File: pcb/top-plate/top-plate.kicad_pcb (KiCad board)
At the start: 2 copper layers, 285.8 x 114.3 mm, 81 parts

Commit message: Add the remaining M2 holes for the top plate
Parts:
- added REF**: MountingHole_2.2mm_M2, MountingHole:MountingHole_2.2mm_M2, F.Cu at (38.1, 30.3)
- added REF**: MountingHole_2.2mm_M2, MountingHole:MountingHole_2.2mm_M2, F.Cu at (285.7, 126.4)
- added REF**: MountingHole_2.2mm_M2, MountingHole:MountingHole_2.2mm_M2, F.Cu at (38.1, 126.4)
- added REF**: MountingHole_2.2mm_M2, MountingHole:MountingHole_2.2mm_M2, F.Cu at (285.7, 30.3)
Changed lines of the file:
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@@
     (fp_line (start -6.5 7) (end 6.499672 7.000007) (layer "Edge.Cuts") (width 0.1))
     (fp_arc (start 53 -6) (mid 53.353553 -5.853553) (end 53.5 -5.5) (layer "Edge.Cuts") (width 0.1))
-    (fp_arc (start 6.999672 5.500007) (mid 7.146108 5.146445) (end 7.499672 5.000007) (layer "Edge.Cuts") (width 0.1))
+    (fp_arc (start 6.999672 5.500007) (mid 7.146107 5.146441) (end 7.499672 5.000007) (layer "Edge.Cuts") (width 0.1))
     (fp_arc (start 47.975 6.5) (mid 48.328553 6.646447) (end 48.475 7) (layer "Edge.Cuts") (width 0.1))
     (fp_arc (start 46.25 5) (mid 46.603553 5.146447) (end 46.75 5.5) (layer "Edge.Cuts") (width 0.1))
@@
     (fp_arc (start -53 6.5) (mid -53.353553 6.353553) (end -53.5 6) (layer "Edge.Cuts") (width 0.1))
     (fp_arc (start -7 -5.5) (mid -7.146447 -5.146447) (end -7.5 -5) (layer "Edge.Cuts") (width 0.1))
-    (fp_arc (start 6.999672 6.500007) (mid 6.853215 6.853551) (end 6.499672 7.000007) (layer "Edge.Cuts") (width 0.1))
+    (fp_arc (start 6.999672 6.500007) (mid 6.853214 6.853548) (end 6.499672 7.000007) (layer "Edge.Cuts") (width 0.1))
     (fp_arc (start 51.775 7) (mid 51.921447 6.646447) (end 52.275 6.5) (layer "Edge.Cuts") (width 0.1))
     (fp_arc (start -53.5 -5.5) (mid -53.353553 -5.853553) (end -53 -6) (layer "Edge.Cuts") (width 0.1))
@@
     (fp_arc (start -7 -6.5) (mid -6.853553 -6.853553) (end -6.5 -7) (layer "Edge.Cuts") (width 0.1))
   )
+  (footprint "MountingHole:MountingHole_2.2mm_M2" (layer "F.Cu")
+    (at 38.1 30.3)
+    (descr "Mounting Hole 2.2mm, no annular, M2")
+    (tags "mounting hole 2.2mm no annular m2")
+    (attr exclude_from_pos_files exclude_from_bom)
+    (fp_text reference "REF**" (at 0 -3.2) (layer "F.SilkS")
+      (effects (font (size 1 1) (thickness 0.15)))
+    )
+    (fp_text value "MountingHole_2.2mm_M2" (at 0 3.2) (layer "F.Fab")
+      (effects (font (size 1 1) (thickness 0.15)))
+    )
+    (fp_text user "${REFERENCE}" (at 0 0) (layer "F.Fab")
+      (effects (font (size 1 1) (thickness 0.15)))
+    )
+    (fp_circle (center 0 0) (end 2.2 0) (layer "Cmts.User") (width 0.15) (fill none))
+    (fp_circle (center 0 0) (end 2.45 0) (layer "F.CrtYd") (width 0.05) (fill none))
+    (pad "" np_thru_hole circle (at 0 0) (size 2.2 2.2) (drill 2.2) (layers *.Cu *.Mask))
+  )
   (footprint "bschwind_slots:mx_top_plate_1.00u" (layer "F.Cu")
     (at 228.6 66.67505)
@@
     (fp_arc (start -6.5 6.990924) (mid -6.853553 6.844477) (end -7 6.490924) (layer "Edge.Cuts") (width 0.1))
   )
+  (footprint "MountingHole:MountingHole_2.2mm_M2" (layer "F.Cu")
+    (at 285.7 126.4)
+    (descr "Mounting Hole 2.2mm, no annular, M2")
+    (tags "mounting hole 2.2mm no annular m2")
+    (attr exclude_from_pos_files exclude_from_bom)
+    (fp_text reference "REF**" (at 0 -3.2) (layer "F.SilkS")
+      (effects (font (size 1 1) (thickness 0.15)))
+    )
+    (fp_text value "MountingHole_2.2mm_M2" (at 0 3.2) (layer "F.Fab")
+      (effects (font (size 1 1) (thickness 0.15)))
+    )
+    (fp_text user "${REFERENCE}" (at 0 0) (layer "F.Fab")
+      (effects (font (size 1 1) (thickness 0.15)))
+    )
+    (fp_circle (center 0 0) (end 2.2 0) (layer "Cmts.User") (width 0.15) (fill none))
+    (fp_circle (center 0 0) (end 2.45 0) (layer "F.CrtYd") (width 0.05) (fill none))
+    (pad "" np_thru_hole circle (at 0 0) (size 2.2 2.2) (drill 2.2) (layers *.Cu *.Mask))
+  )
   (footprint "bschwind_slots:mx_top_plate_1.00u" (layer "F.Cu")
     (at 171.45 28.57505)
@@
     (fp_arc (start -7 -6.5) (mid -6.853553 -6.853553) (end -6.5 -7) (layer "Edge.Cuts") (width 0.1))
   )
+  (footprint "MountingHole:MountingHole_2.2mm_M2" (layer "F.Cu")
+    (at 38.1 126.4)
+    (descr "Mounting Hole 2.2mm, no annular, M2")
+    (tags "mounting hole 2.2mm no annular m2")
+    (attr exclude_from_pos_files exclude_from_bom)
+    (fp_text reference "REF**" (at 0 -3.2) (layer "F.SilkS")
+      (effects (font (size 1 1) (thickness 0.15)))
+    )
+    (fp_text value "MountingHole_2.2mm_M2" (at 0 3.2) (layer "F.Fab")
+      (effects (font (size 1 1) (thickness 0.15)))
+    )
+    (fp_text user "${REFERENCE}" (at 0 0) (layer "F.Fab")
+      (effects (font (size 1 1) (thickness 0.15)))
+    )
+    (fp_circle (center 0 0) (end 2.2 0) (layer "Cmts.User") (width 0.15) (fill none))
+    (fp_circle (center 0 0) (end 2.45 0) (layer "F.CrtYd") (width 0.05) (fill none))
+    (pad "" np_thru_hole circle (at 0 0) (size 2.2 2.2) (drill 2.2) (layers *.Cu *.Mask))
+  )
   (footprint "bschwind_slots:mx_top_plate_1.00u" (layer "F.Cu")
     (at 219.075 47.62505)
@@
     (fp_arc (start 6.5 -7) (mid 6.853553 -6.853553) (end 7 -6.5) (layer "Edge.Cuts") (width 0.1))
   )
-  (footprint "bschwind_slots:mx_top_plate_1.00u" (layer "F.Cu")
+  (footprint "MountingHole:MountingHole_2.2mm_M2" (layer "F.Cu")
+    (at 285.7 30.3)
+    (descr "Mounting Hole 2.2mm, no annular, M2")
+    (tags "mounting hole 2.2mm no annular m2")
+    (attr exclude_from_pos_files exclude_from_bom)
+    (fp_text reference "REF**" (at 0 -3.2) (layer "F.SilkS")
+      (effects (font (size 1 1) (thickness 0.15)))
+    )
+    (fp_text value "MountingHole_2.2mm_M2" (at 0 3.2) (layer "F.Fab")
+      (effects (font (size 1 1) (thickness 0.15)))
+    )
+    (fp_text user "${REFERENCE}" (at 0 0) (layer "F.Fab")
+      (effects (font (size 1 1) (thickness 0.15)))
+    )
+    (fp_circle (center 0 0) (end 2.2 0) (layer "Cmts.User") (width 0.15) (fill none))
+    (fp_circle (center 0 0) (end 2.45 0) (layer "F.CrtYd") (width 0.05) (fill none))
+    (pad "" np_thru_hole circle (at 0 0) (size 2.2 2.2) (drill 2.2) (layers *.Cu *.Mask))
+  )
+  (footprint "bschwind_slots:mx_top_plate_1.00u" (layer "F.Cu")

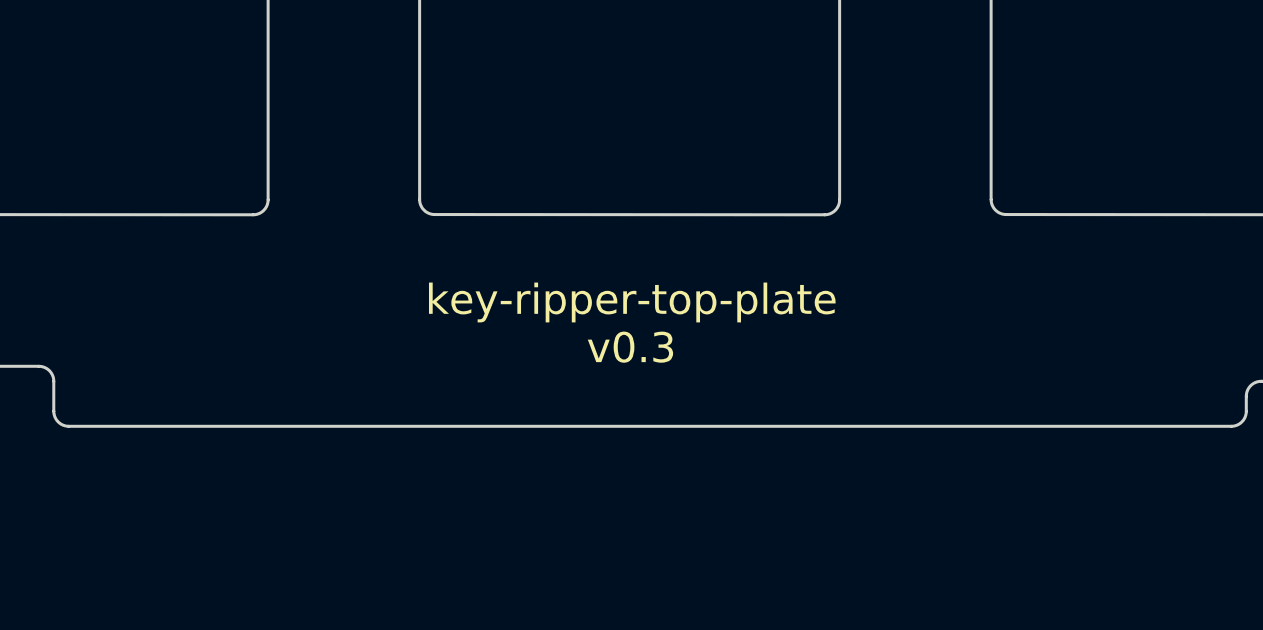
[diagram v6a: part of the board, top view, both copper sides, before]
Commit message: Update silkscreens on the plates
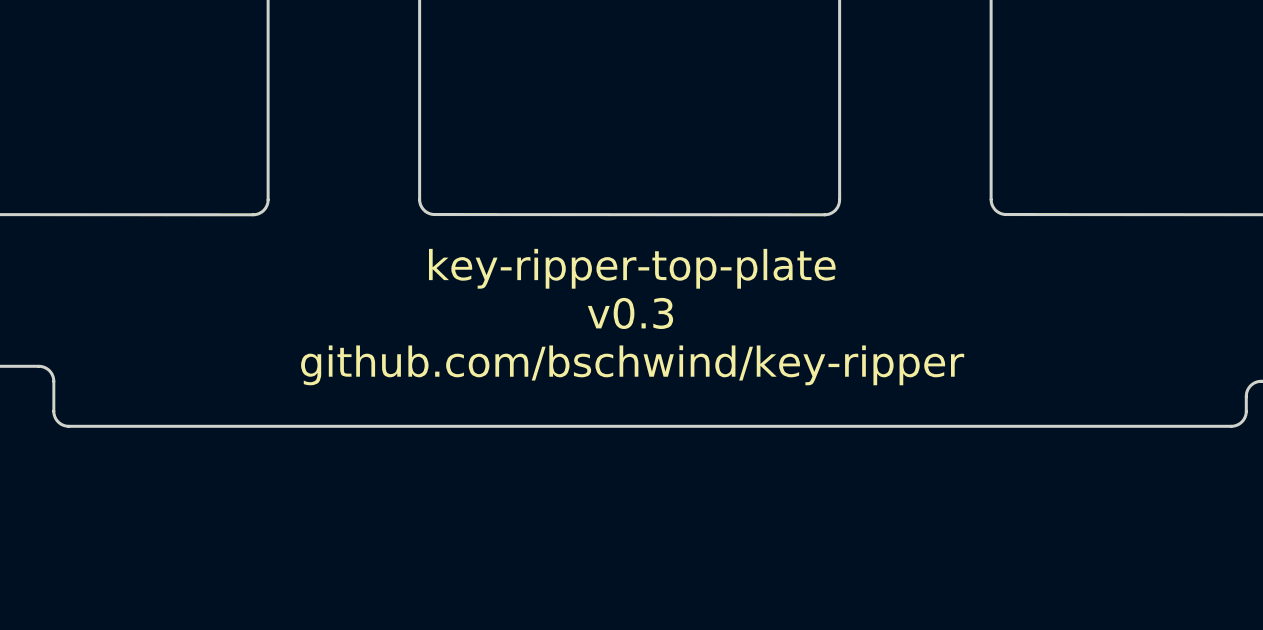
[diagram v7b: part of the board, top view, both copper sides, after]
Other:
- board text added: "key-ripper-top-plate v0.3 github.com/bschwind/key-ripper"
- board text removed: "key-ripper-top-plate v0.3"
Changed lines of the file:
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@@
     (fp_line (start -6.5 7) (end 6.499672 7.000007) (layer "Edge.Cuts") (width 0.1))
     (fp_arc (start 53 -6) (mid 53.353553 -5.853553) (end 53.5 -5.5) (layer "Edge.Cuts") (width 0.1))
-    (fp_arc (start 6.999672 5.500007) (mid 7.146107 5.146441) (end 7.499672 5.000007) (layer "Edge.Cuts") (width 0.1))
+    (fp_arc (start 6.999672 5.500007) (mid 7.146108 5.146445) (end 7.499672 5.000007) (layer "Edge.Cuts") (width 0.1))
     (fp_arc (start 47.975 6.5) (mid 48.328553 6.646447) (end 48.475 7) (layer "Edge.Cuts") (width 0.1))
     (fp_arc (start 46.25 5) (mid 46.603553 5.146447) (end 46.75 5.5) (layer "Edge.Cuts") (width 0.1))
@@
     (fp_arc (start -53 6.5) (mid -53.353553 6.353553) (end -53.5 6) (layer "Edge.Cuts") (width 0.1))
     (fp_arc (start -7 -5.5) (mid -7.146447 -5.146447) (end -7.5 -5) (layer "Edge.Cuts") (width 0.1))
-    (fp_arc (start 6.999672 6.500007) (mid 6.853214 6.853548) (end 6.499672 7.000007) (layer "Edge.Cuts") (width 0.1))
+    (fp_arc (start 6.999672 6.500007) (mid 6.853215 6.853551) (end 6.499672 7.000007) (layer "Edge.Cuts") (width 0.1))
     (fp_arc (start 51.775 7) (mid 51.921447 6.646447) (end 52.275 6.5) (layer "Edge.Cuts") (width 0.1))
     (fp_arc (start -53.5 -5.5) (mid -53.353553 -5.853553) (end -53 -6) (layer "Edge.Cuts") (width 0.1))
@@
   (gr_line (start 304.8 21.4313) (end 304.8 130.9688) (layer "Edge.Cuts") (width 0.1))
   (gr_arc (start 304.8 130.9688) (mid 304.102516 132.652551) (end 302.41875 133.35005) (layer "Edge.Cuts") (width 0.1))
-  (gr_text "key-ripper-top-plate\nv0.3" (at 185.8 115.4188) (layer "F.SilkS")
+  (gr_text "key-ripper-top-plate\nv0.3\ngithub.com/bschwind/key-ripper" (at 185.8 115.1) (layer "F.SilkS")
     (effects (font (size 1 1) (thickness 0.15)))
   )

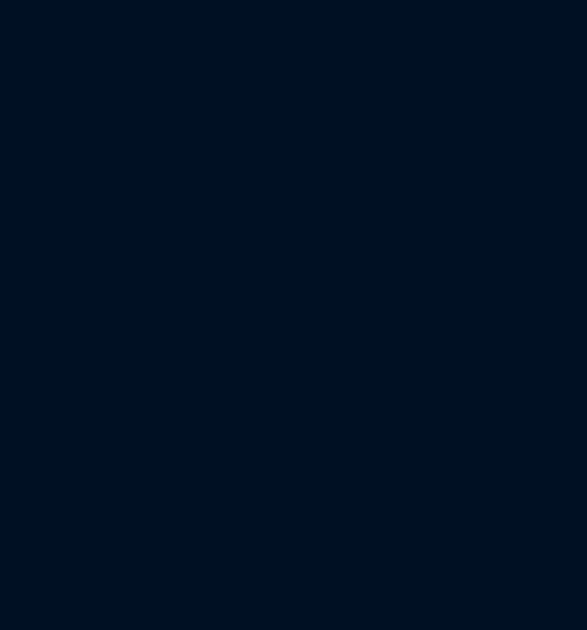
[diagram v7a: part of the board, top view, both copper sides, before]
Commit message: Add some patterns to the top and bottom plate copper pours
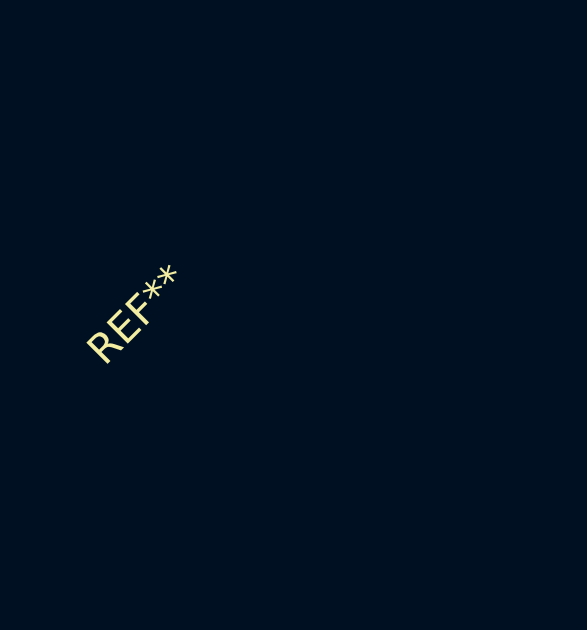
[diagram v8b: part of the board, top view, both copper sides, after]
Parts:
- added REF**: 2mm-bars-0.3mm-gap, copper-pour-patterns:2mm-bars-0.3mm-gap, F.Cu at (-52.6, 73.1)
